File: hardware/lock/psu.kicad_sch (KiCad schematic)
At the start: 11 parts, among them Q2 AO3400A, U2 MT3608

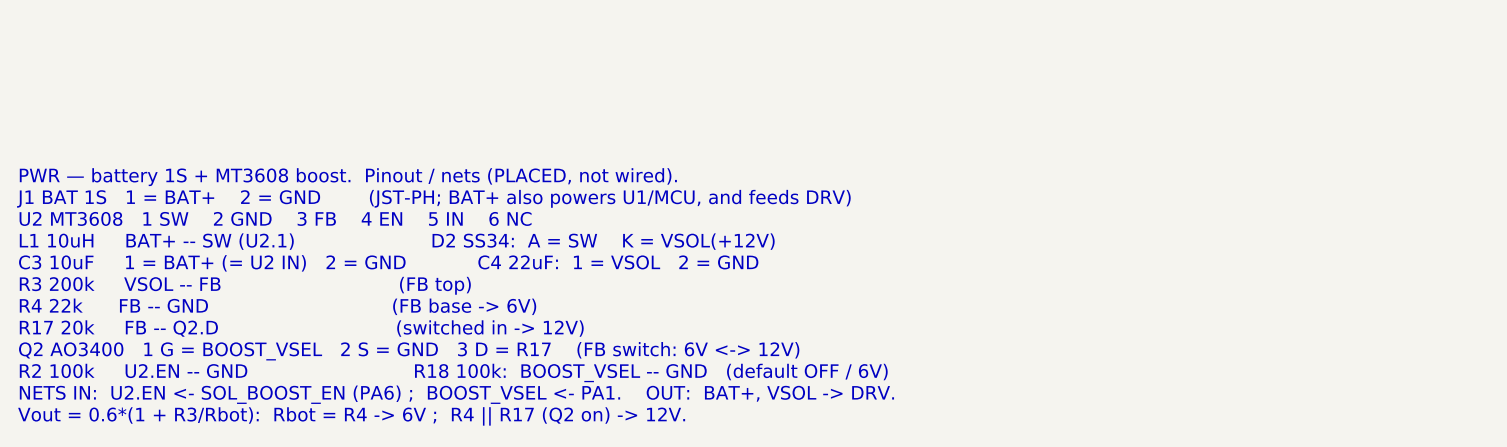
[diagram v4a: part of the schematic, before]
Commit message: hardware: fix PSU load-share S/D, make all sheet notes monospace
The PSU wiring note specified Q1 (AO3401A load-share PMOS) as S=BAT+,
D=VSYS. A PMOS body diode conducts D->S, so that orientation points the
diode VSYS -> BAT+: with USB attached VSYS sits ~4.7V (VBUS - D3) against
a 3.0-4.2V cell, forward-biasing it and dumping uncontrolled current into
the battery, bypassing the MCP73831 charger entirely.

Correct assignment is D=BAT+, S=VSYS, so the body diode points BAT+ ->
VSYS: the battery always reaches the load, and USB can never back-feed
the cell. Q1 was placed but never wired (all three pins are unconnected
in the netlist), so this is a spec fix ahead of wiring, not a board
change. The lock's Q3 is a high-side switch and deliberately uses the
opposite S/D assignment; the note now says so, to stop the two being
"reconciled" by pattern-matching.

Also relaid the PSU note as a two-column table and gave every sheet note
the Courier New face the generator already emits (kschgen NOTE_FONT, added
in 43a6067). The sheets predate that commit, so their notes rendered in
KiCad's variable-width stroke font and the space-padded pin tables did not
line up. Font only on the other six notes -- text is untouched.

Verified: kicad-cli netlists for both boards are byte-identical before and
after (ephemerkey 259 nodes, lock 131 nodes) once the export timestamp is
excluded; no non-font lines changed in any sheet; all sheets re-rendered
and the notes fit inside the page frame.

The four ephemerkey sheets also carry pre-existing eeschema reformatting
(expanded lib_symbols) that was already in the working tree.

Co-Authored-By: Claude Opus 4.8 (1M context) <noreply@anthropic.com>
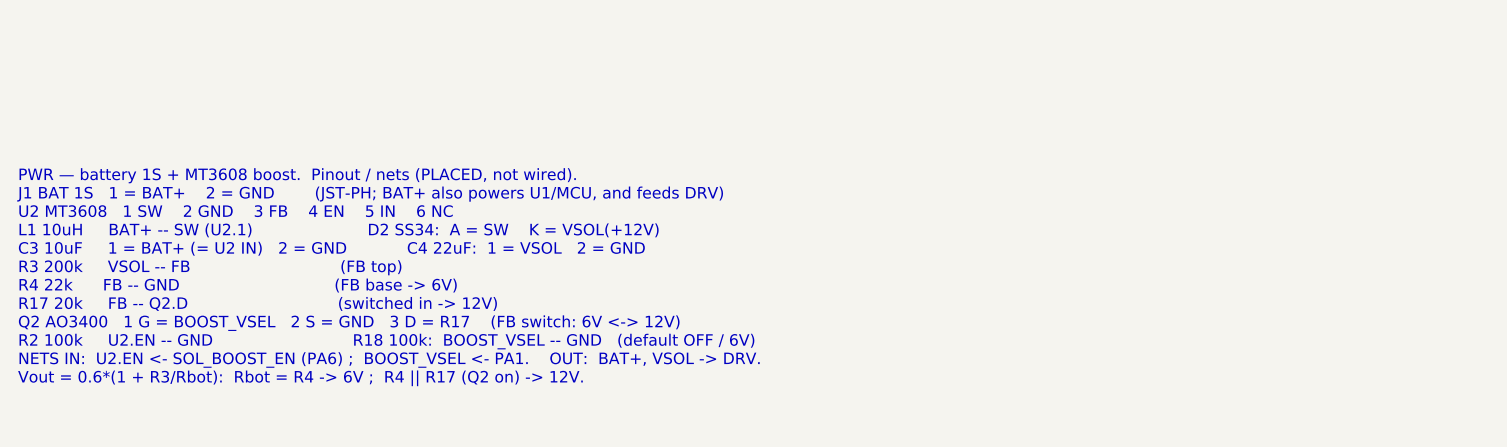
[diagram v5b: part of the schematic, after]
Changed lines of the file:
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@@
 		(effects
 			(font
-				(size 1.5 1.5)
+				(face "Courier New")
+				(size 1.27 1.27)
 			)
 			(justify left top)
